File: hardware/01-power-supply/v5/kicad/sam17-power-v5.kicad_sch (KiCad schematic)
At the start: 208 parts, among them J1 Bornera 2P 5.0 mm, J10 PinHeader 1x04, J2 Molex KK-254 4P, J3 Bornera 4P 5.08 mm, J5 Faston 6.3x0.8 PCB, J6 Molex KK-254 2P, J7 Molex KK-254 4P, J8 PinHeader 1x04, J9 Molex KK-254 2P, Q2 CSD18534Q5A, Q3 MMBT3906, Q4 MMBT3906, Q5 MMBT3906, Q6 MMBT3906, SW1 Pulsador 6x6, U1 LT1963AEQ, U10 ADS1115IDGS, U11 TMP1075DGK, U12 INA226, U13 INA226, U14 INA226, U15 LM74502DDFR, U16 TPS26631PWPR, U17 MSP430FR2111IPW16, U18 TPS70933DBVR, U19 TPS26631PWPR, U2 LT3015EQ, U20 LM393B, U21 TL431BI, U22 TL431BI, U23 TL431BI, U24 TL431BI, U25 TL431BI, U4 LT3045EDD, U5 LT3045EDD, U6 LT3094EDD, U7 LT3094EDD, U8 INA226, U9 ISO1541

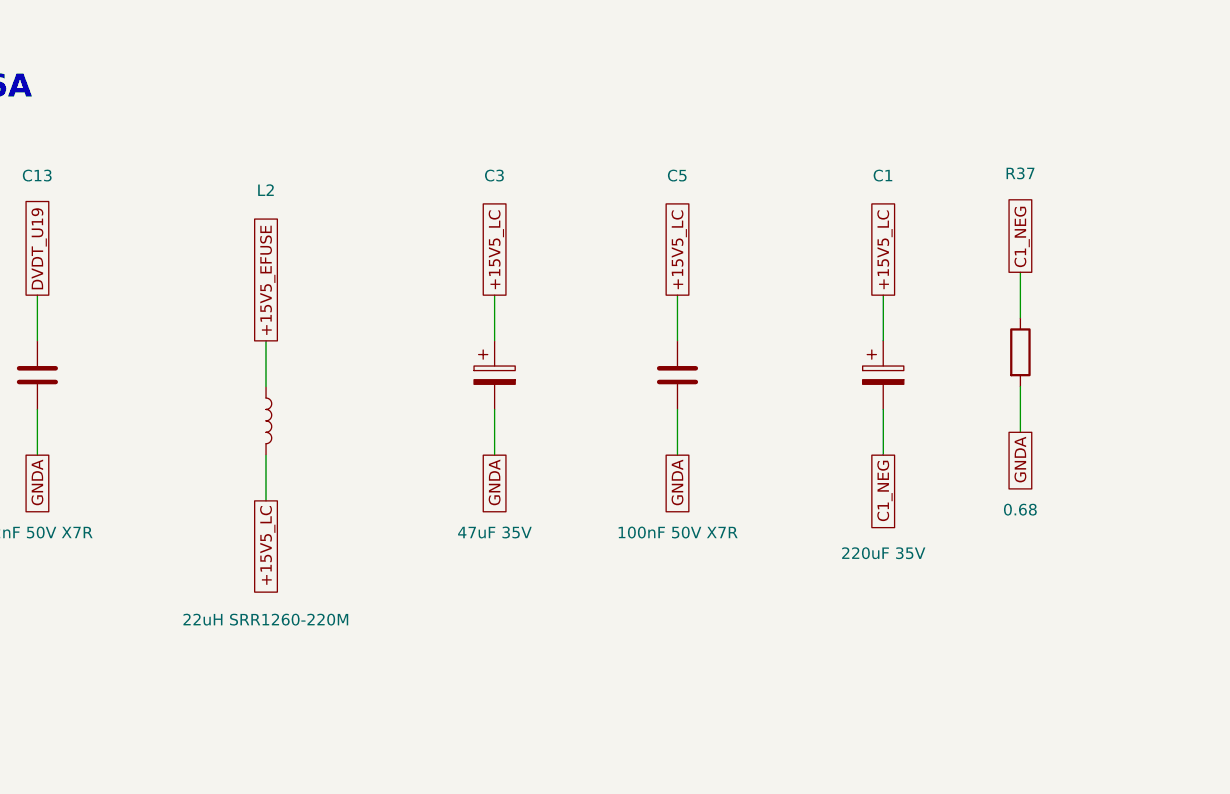
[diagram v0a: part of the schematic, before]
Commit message: hardware: fuente v5, placa y fabricacion con L2 en SRP1265A-220M
Placa colocada y ruteada de nuevo: Freerouting en 3 rondas y el rescate
cierra las 7 conexiones que deja abiertas. L2 sigue en (97, 48); su
cuerpo pasa de 12,5 a 13,5 mm en x.

build_pcb.py: Freerouting salio de U4.9 por su cuenta y puso la via a
mitad de la salida fija de OUTS_POS, con 0,8 mm de punta colgando.
limpiar_colgantes() ya no deja asi una pista fija: la recorta hasta el
ultimo contacto de su red (_recortar), y lo de antes no cambia.

- 1510 pistas y 284 vias (263 de 0,6/0,3 mm y 21 de 0,8/0,4 mm).
- Bajo el cuerpo de L2 pasan ahora +15V5_FILT en F.Cu, entre sus pads, y
  SCL_A/SDA_A en In2, debajo del plano de In1.
- DRC (kicad-cli 10.0.3, todas las severidades, zonas rellenas y paridad
  con el esquematico): 0 infracciones, 0 sin conectar, 0 de paridad.
- Ocho referencias van solo en F.Fab: entran R43, R70, R71 y FB1, y R40
  y R67 vuelven a la serigrafia.

Esquematico, netlist, fab/ y pcb/ regenerados.
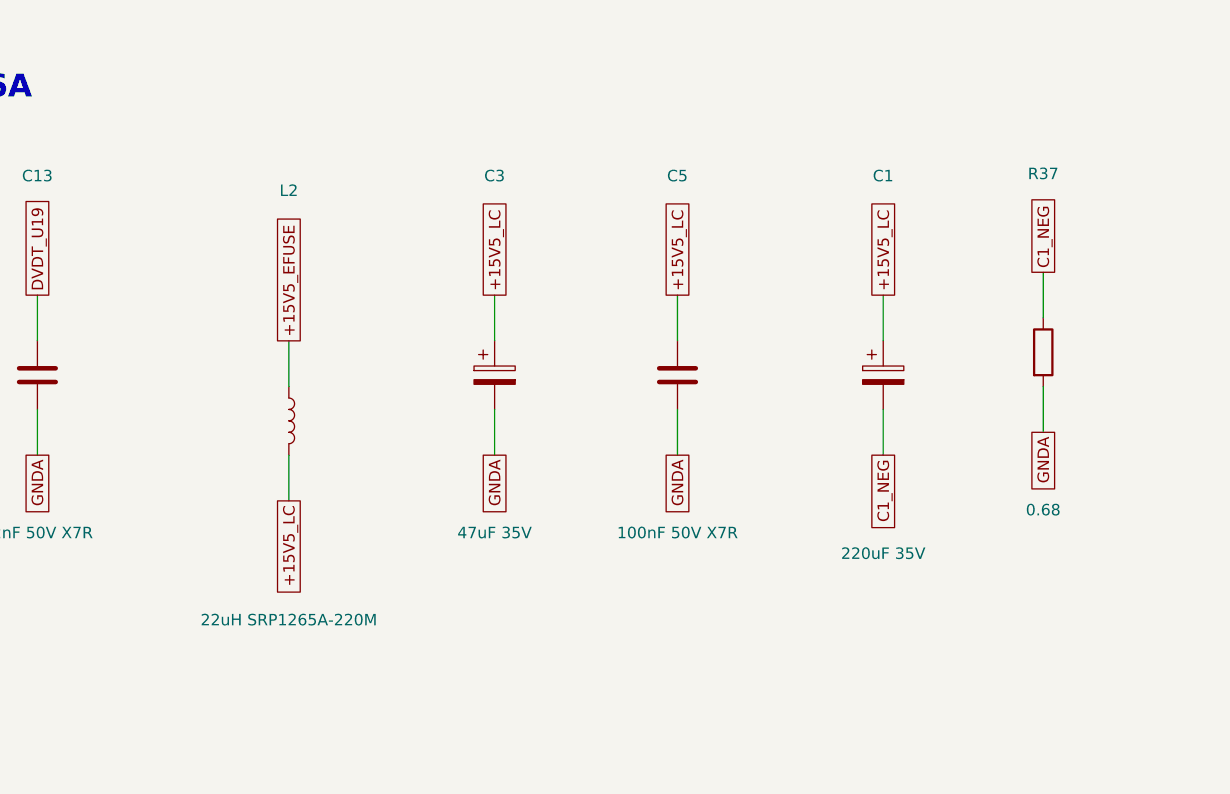
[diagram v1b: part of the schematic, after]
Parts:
- L2: value 22uH SRR1260-220M -> 22uH SRP1265A-220M; footprint Inductor_SMD:L_Bourns_SRR1260 -> sam17:L_Bourns_SRP1265A; LCSC C3224283 -> C2041465; MPN SRR1260-220M -> SRP1265A-220M
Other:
- moved on the sheet: L2, R37
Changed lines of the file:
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@@
 	(wire
 		(pts
-			(xy 241.3 422.91) (xy 241.3 417.83)
+			(xy 243.84 422.91) (xy 243.84 417.83)
 		)
 		(stroke
@@
 	(wire
 		(pts
-			(xy 241.3 430.53) (xy 241.3 435.61)
+			(xy 243.84 430.53) (xy 243.84 435.61)
 		)
 		(stroke
@@
 	(wire
 		(pts
-			(xy 325.12 415.29) (xy 325.12 410.21)
+			(xy 327.66 415.29) (xy 327.66 410.21)
 		)
 		(stroke
@@
 	(wire
 		(pts
-			(xy 325.12 422.91) (xy 325.12 427.99)
+			(xy 327.66 422.91) (xy 327.66 427.99)
 		)
 		(stroke
@@
 	(global_label "+15V5_EFUSE"
 		(shape passive)
-		(at 241.3 417.83 90)
+		(at 243.84 417.83 90)
 		(effects
 			(font
@@
 	(global_label "+15V5_LC"
 		(shape passive)
-		(at 241.3 435.61 270)
+		(at 243.84 435.61 270)
 		(effects
 			(font
@@
 	(global_label "C1_NEG"
 		(shape passive)
-		(at 325.12 410.21 90)
+		(at 327.66 410.21 90)
 		(effects
 			(font
@@
 	(global_label "GNDA"
 		(shape passive)
-		(at 325.12 427.99 270)
+		(at 327.66 427.99 270)
 		(effects
 			(font
@@
 	(symbol
 		(lib_id "Device:L")
-		(at 241.3 426.72 0)
+		(at 243.84 426.72 0)
 		(unit 1)
 		(exclude_from_sim no)
@@
 		(dnp no)
 		(property "Reference" "L2"
-			(at 241.3 401.14 0)
+			(at 243.84 401.14 0)
 			(show_name no)
 			(do_not_autoplace no)
@@
 			)
 		)
-		(property "Value" "22uH SRR1260-220M"
-			(at 241.3 448.85 0)
+		(property "Value" "22uH SRP1265A-220M"
+			(at 243.84 448.85 0)
 			(show_name no)
 			(do_not_autoplace no)
@@
 			)
 		)
-		(property "Footprint" "Inductor_SMD:L_Bourns_SRR1260"
-			(at 241.3 426.72 0)
+		(property "Footprint" "sam17:L_Bourns_SRP1265A"
+			(at 243.84 426.72 0)
 			(hide yes)
 			(show_name no)
@@
 		)
 		(property "Datasheet" ""
-			(at 241.3 426.72 0)
+			(at 243.84 426.72 0)
 			(hide yes)
 			(show_name no)
@@
 		)
 		(property "Description" ""
-			(at 241.3 426.72 0)
+			(at 243.84 426.72 0)
 			(hide yes)
 			(show_name no)
@@
 			)
 		)
-		(property "LCSC" "C3224283"
-			(at 241.3 426.72 0)
+		(property "LCSC" "C2041465"
+			(at 243.84 426.72 0)
 			(hide yes)
 			(show_name no)
@@
 			)
 		)
-		(property "MPN" "SRR1260-220M"
-			(at 241.3 426.72 0)
+		(property "MPN" "SRP1265A-220M"
+			(at 243.84 426.72 0)
 			(hide yes)
 			(show_name no)
@@
 	(symbol
 		(lib_id "Device:R")
-		(at 325.12 419.1 0)
+		(at 327.66 419.1 0)
 		(unit 1)
 		(exclude_from_sim no)
@@
 		(dnp no)
 		(property "Reference" "R37"
-			(at 325.12 399.27 0)
+			(at 327.66 399.27 0)
 			(show_name no)
 			(do_not_autoplace no)
@@
 		)
 		(property "Value" "0.68"
-			(at 325.12 436.63 0)
+			(at 327.66 436.63 0)
 			(show_name no)
 			(do_not_autoplace no)
@@
 		)
 		(property "Footprint" "Resistor_SMD:R_1206_3216Metric"
-			(at 325.12 419.1 0)
+			(at 327.66 419.1 0)
 			(hide yes)
 			(show_name no)
@@
 		)
 		(property "Datasheet" ""
-			(at 325.12 419.1 0)
+			(at 327.66 419.1 0)
 			(hide yes)
 			(show_name no)
@@
 		)
 		(property "Description" ""
-			(at 325.12 419.1 0)
+			(at 327.66 419.1 0)
 			(hide yes)
 			(show_name no)
@@
 		)
 		(property "LCSC" "C19108"
-			(at 325.12 419.1 0)
+			(at 327.66 419.1 0)
 			(hide yes)
 			(show_name no)
@@
 		)
 		(property "MPN" "1206W4F680LT5E"
-			(at 325.12 419.1 0)
+			(at 327.66 419.1 0)
 			(hide yes)
 			(show_name no)

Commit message: fix(fuente-v5): PS3 a THN 20-2411WI aislado, con C39 y +5V_AUX tras F4
El K7805T de PS3 era un buck no aislado: con la entrada puenteada a la
salida, +5V_AUX pasaba de los 6,0 V de los INA226 y del ISO1541. En el
THN 20-2411WI la entrada y la salida solo se tocan por la barrera de
1600 VDC, el camino que la propuesta de piezas (sec. 9.1) deja fuera del
contrato de fallo simple.

- C39, 1000 uF / 16 V (Lelon VZH102M1CTR-1010, C249844): con el THN a su
  limite la subida del riel baja a 0,0095 V/us y el pico queda en 5,88 V.
- +5V_AUX cuelga de +5V_FUSED_RACK: si F4 abre tras el disparo, se apaga
  en vez de quedarse con el OVP del THN (hasta 8,20 V).
- R49 = 12,7 kohm: SCR3 dispara entre 5,53 y 5,86 V.
- check_absmax.py: fuga_ps3() con su guarda y sus canarios, y la fila de
  +5V_AUX en absmax.csv. check_netlist.py fija la toma de R20 tras F4.
- Placa reruteada: PS3 en la columna de convertidores, PS2 abajo, NT1
  entre PS5 y PS3, GNDA por la derecha de PS3 y C39. DRC 0, 0 sin conectar.
- Presupuestos: derating del 2411WI, 83 % al 20 % de carga (el cajon pasa
  a 65,31 W), medidas.csv.
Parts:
- removed C15: 10uF 50V X7R, Capacitor_SMD:C_1210_3225Metric, symbol Device:C
- added C39: 1000uF 16V, Capacitor_SMD:CP_Elec_10x10, symbol Device:C_Polarized
- PS3: value K7805T-1000R3 -> THN 20-2411WI; footprint sam17:Converter_DCDC_Mornsun_K78_T-1000R3_SMD -> Converter_DCDC:Converter_DCDC_TRACO_THL30-xxxxWI_THT; symbol sam17:Mornsun_K78xxT-1000R3 -> sam17:TRACO_THN_Single; MPN K7805T-1000R3 -> THN 20-2411WI
- R49: value 13.3k 0.1% -> 12.7k 0.1%; LCSC C865182 -> C50670219; MPN RT0805BRD0713K3L -> TC0525B1272T5G
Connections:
- net +24V_SW: no longer PS3.2 (+Vin)
- net +5V_FUSED_RACK: now also R20.1, U12.10 (Vin+)
- net +5V_RAW_RACK: now also PS3.3 (+Vout), C39.1; no longer PS3.4 (+Vout), PS3.5 (+Vout), R20.1, U12.10 (Vin+)
- net GND24: now also PS3.2 (-Vin); no longer C16.2, PS3.3 (GND), PS3.7 (GND)
- net GNDA: now also C16.2, PS3.5 (-Vout), C39.2
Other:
- note added: "BLOQUE DCDC: Convertidores: THN 30 (+-12 rack), URB (+5 digital M1), 3 x THN 20 (+5 rack, +-15.5)"
- note removed: "BLOQUE DCDC: Convertidores: THN 30 (+-12 rack), URB (+5 digital M1), K78 (+5 rack), 2 x THN 20 (+-15.5)"
- moved on the sheet: C16, C2, C22, C24, C25, C26, C28, C35, C37, C4, C6, D10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

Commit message: feat(fuente-v5): placa y ficheros de fabricacion con Q7 en el retorno
Regenerados con build_schematic.py, build_pcb.py y build_fab.py: DRC con
todas las severidades y paridad con el esquematico en 0 infracciones, 0 sin
conectar y 0 diferencias de paridad; 1464 pistas y 294 vias (271 de 0,6 mm y
23 de 0,8 mm).

- Q7 sobre J1.2 (rot 270, drenador abajo) y D1 a su lado; la isla
  RET24_RAW (J1.2, D1.2 y el drenador de Q7) es cobre fijo de >= 2,4 mm que
  los vertidos de GND24 rodean sin tocar, y las tres fuentes de Q7 van
  juntas a GND24 por cobre de 1,8 mm. R85 y D20 quedan junto a D1.
- L3 en la huella de la SRP1265A (13,5 x 12,5 mm).
- fab/: gerbers, taladros y posiciones; el BOM y el CPL de JLC pierden D10 y
  D12 (sin montar) y ganan Q7, D20 y R85. Nueve referencias solo en F.Fab.
- sam17-power-v5.net, .kicad_sch, esquemas y vistas de la placa.
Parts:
- added D20: BZT52C15, Diode_SMD:D_SOD-123, symbol Device:D_Zener
- added Q7: CSD18534Q5A, Package_TO_SOT_SMD:TDSON-8-1, symbol Transistor_FET:CSD18534Q5A
- added R85: 10k, Resistor_SMD:R_0805_2012Metric, symbol Device:R
- C10: value 100nF 50V X7R -> 100nF 100V X7R; LCSC C49678 -> C106243; MPN CC0805KRX7R9BB104 -> CC0805KKX7R0BB104
- D1: value SMBJ26CA -> SMBJ33CA; LCSC C83332 -> C83325; MPN SMBJ26CA -> SMBJ33CA
- L3: value 22uH SRR1260-220M -> 22uH SRP1265A-220M; footprint Inductor_SMD:L_Bourns_SRR1260 -> sam17:L_Bourns_SRP1265A; LCSC C3224283 -> C2041465; MPN SRR1260-220M -> SRP1265A-220M
- R32, R33: value 45.3k -> 45.3k 0.1%; LCSC C17701 -> C866072; MPN 0805W8F4532T5E -> RT0805BRE0745K3L
- R64: value 1k -> 1.2k; LCSC C17513 -> C17379; MPN 0805W8F1001T5E -> 0805W8F1201T5E
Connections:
- net +24V_RAW: now also R85.1
- net GND24: now also D20.2 (A), Q7.1 (S), Q7.2 (S), Q7.3 (S); no longer D1.2 (A2), J1.2 (Pin_2)
- new net G_Q7: D20.1 (K), Q7.4 (G), R85.2
- new net RET24_RAW: D1.2 (A2), J1.2 (Pin_2), Q7.5 (D)
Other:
- note added: "BLOQUE M5: Entrada 24 V, polaridad (LM74502 + 2 x CSD18534Q5A, +24 V y retorno), eFuse U16 y supervisor M5"
- note removed: "BLOQUE M5: Entrada 24 V, polaridad (LM74502 + CSD18534Q5A), eFuse U16 y supervisor M5"
- moved on the sheet: C10, C11, C12, C23, C6, C7, C8, C9, D11, D18, D2, J10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

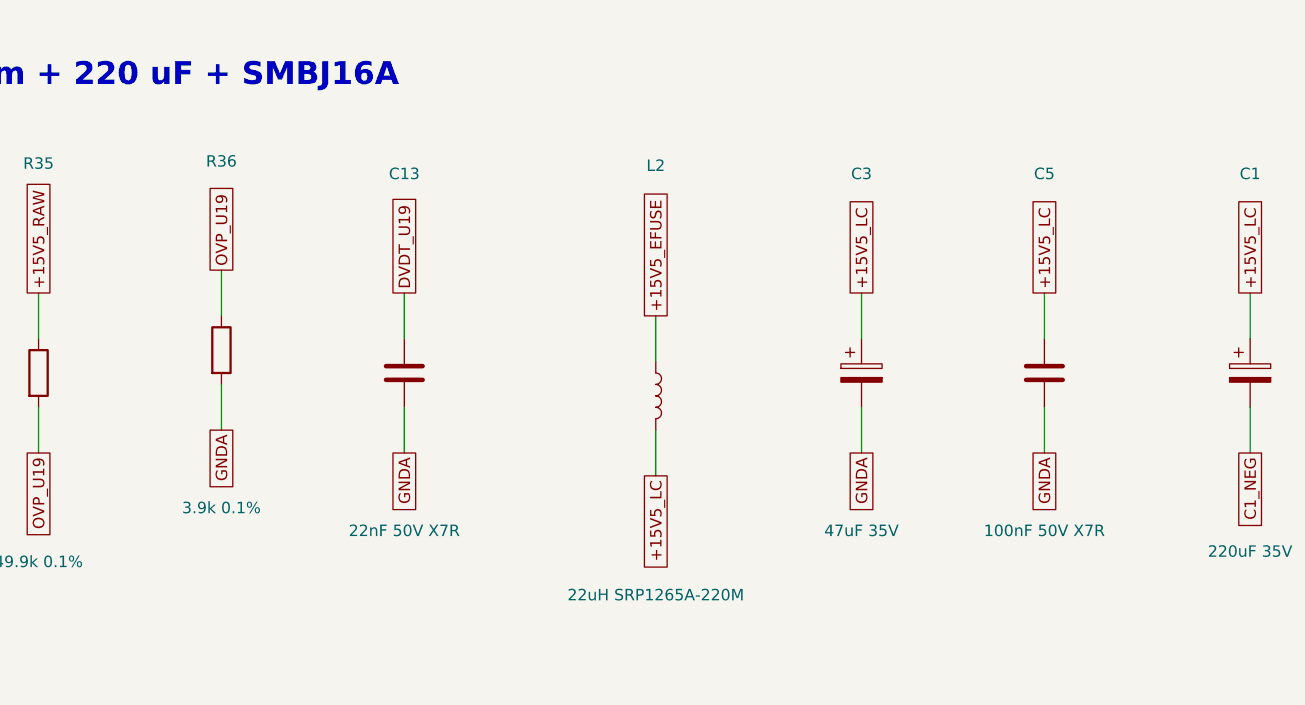
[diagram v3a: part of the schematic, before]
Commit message: fuente-v5: R36 a 3,74 kohm, el OVP de U19 deja sitio al sobreimpulso del THN
R36 pasa de 3,9 kohm a 3,74 kohm 0,1 % (Yageo RT0805BRD073K74L, C865467,
misma serie y huella). El OVP de U19 sube de 16,55 a 17,21 V nominal, con
banda de 16,83 a 17,59 V: el margen sobre el THN sano pasa de 0,18 a 0,82 V
en la envolvente de margen_budget.py, y el sobreimpulso tipico al soltar
carga (~0,19 V) cabe.

Con el borde alto por encima del pico de #334 (17,40 V), lo peor que ve U1
es un THN atascado justo debajo del OVP. check_absmax.py toma el mayor de
los dos en absmax.csv, en la guarda de D10 y en su canario; D10 sigue sin
conducir (17,59 V contra V_BR 17,8 V).

La spec v5 y la propuesta de piezas llevan la banda nueva y las cifras del
disparo rapido (3,32 A, 7,5 us). Placa regenerada con --desde-ruteo: mismo
ruteo, DRC en 0.
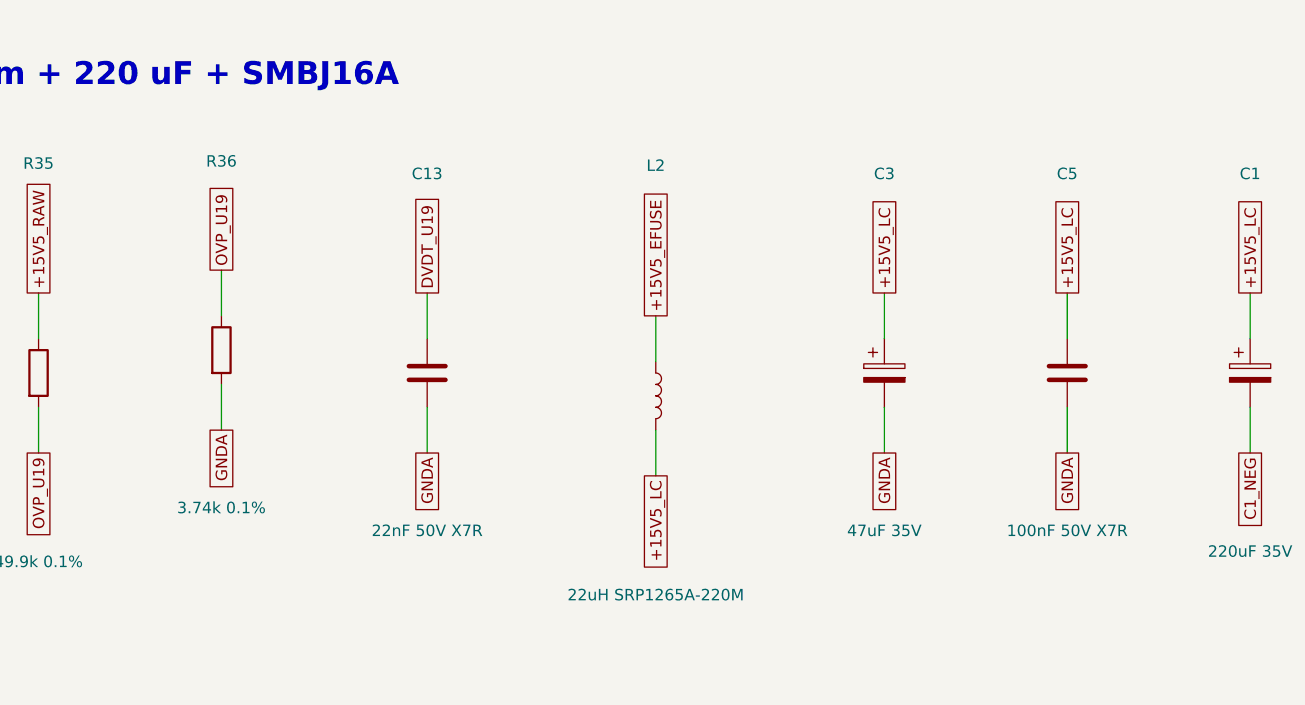
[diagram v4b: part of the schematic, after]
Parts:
- R36: value 3.9k 0.1% -> 3.74k 0.1%; LCSC C865471 -> C865467; MPN RT0805BRD073K9L -> RT0805BRD073K74L
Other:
- moved on the sheet: C13, C3, C5
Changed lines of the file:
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@@
 	(wire
 		(pts
-			(xy 215.9 417.83) (xy 215.9 412.75)
+			(xy 218.44 417.83) (xy 218.44 412.75)
 		)
 		(stroke
@@
 	(wire
 		(pts
-			(xy 215.9 425.45) (xy 215.9 430.53)
+			(xy 218.44 425.45) (xy 218.44 430.53)
 		)
 		(stroke
@@
 	(wire
 		(pts
-			(xy 266.7 417.83) (xy 266.7 412.75)
+			(xy 269.24 417.83) (xy 269.24 412.75)
 		)
 		(stroke
@@
 	(wire
 		(pts
-			(xy 266.7 425.45) (xy 266.7 430.53)
+			(xy 269.24 425.45) (xy 269.24 430.53)
 		)
 		(stroke
@@
 	(wire
 		(pts
-			(xy 287.02 417.83) (xy 287.02 412.75)
+			(xy 289.56 417.83) (xy 289.56 412.75)
 		)
 		(stroke
@@
 	(wire
 		(pts
-			(xy 287.02 425.45) (xy 287.02 430.53)
+			(xy 289.56 425.45) (xy 289.56 430.53)
 		)
 		(stroke
@@
 	(global_label "DVDT_U19"
 		(shape passive)
-		(at 215.9 412.75 90)
+		(at 218.44 412.75 90)
 		(effects
 			(font
@@
 	(global_label "GNDA"
 		(shape passive)
-		(at 215.9 430.53 270)
+		(at 218.44 430.53 270)
 		(effects
 			(font
@@
 	(global_label "+15V5_LC"
 		(shape passive)
-		(at 266.7 412.75 90)
+		(at 269.24 412.75 90)
 		(effects
 			(font
@@
 	(global_label "GNDA"
 		(shape passive)
-		(at 266.7 430.53 270)
+		(at 269.24 430.53 270)
 		(effects
 			(font
@@
 	(global_label "+15V5_LC"
 		(shape passive)
-		(at 287.02 412.75 90)
+		(at 289.56 412.75 90)
 		(effects
 			(font
@@
 	(global_label "GNDA"
 		(shape passive)
-		(at 287.02 430.53 270)
+		(at 289.56 430.53 270)
 		(effects
 			(font
@@
 			)
 		)
-		(property "Value" "3.9k 0.1%"
+		(property "Value" "3.74k 0.1%"
 			(at 195.58 436.63 0)
 			(show_name no)
@@
 			)
 		)
-		(property "LCSC" "C865471"
+		(property "LCSC" "C865467"
 			(at 195.58 419.1 0)
 			(hide yes)
@@
 			)
 		)
-		(property "MPN" "RT0805BRD073K9L"
+		(property "MPN" "RT0805BRD073K74L"
 			(at 195.58 419.1 0)
 			(hide yes)
@@
 	(symbol
 		(lib_id "Device:C")
-		(at 215.9 421.64 0)
+		(at 218.44 421.64 0)
 		(unit 1)
 		(exclude_from_sim no)
@@
 		(dnp no)
 		(property "Reference" "C13"
-			(at 215.9 399.51 0)
+			(at 218.44 399.51 0)
 			(show_name no)
 			(do_not_autoplace no)
@@
 		)
 		(property "Value" "22nF 50V X7R"
-			(at 215.9 439.17 0)
+			(at 218.44 439.17 0)
 			(show_name no)
 			(do_not_autoplace no)
@@
 		)
 		(property "Footprint" "Capacitor_SMD:C_0805_2012Metric"
-			(at 215.9 421.64 0)
+			(at 218.44 421.64 0)
 			(hide yes)
 			(show_name no)
@@
 		)
 		(property "Datasheet" ""
-			(at 215.9 421.64 0)
+			(at 218.44 421.64 0)
 			(hide yes)
 			(show_name no)
@@
 		)
 		(property "Description" ""
-			(at 215.9 421.64 0)
+			(at 218.44 421.64 0)
 			(hide yes)
 			(show_name no)
@@
 		)
 		(property "LCSC" "C1729"
-			(at 215.9 421.64 0)
+			(at 218.44 421.64 0)
 			(hide yes)
 			(show_name no)
@@
 		)
 		(property "MPN" "CL21B223KBANNNC"
-			(at 215.9 421.64 0)
+			(at 218.44 421.64 0)
 			(hide yes)
 			(show_name no)
@@
 	(symbol
 		(lib_id "Device:C_Polarized")
-		(at 266.7 421.64 0)
+		(at 269.24 421.64 0)
 		(unit 1)
 		(exclude_from_sim no)
@@
 		(dnp no)
 		(property "Reference" "C3"
-			(at 266.7 399.51 0)
+			(at 269.24 399.51 0)
 			(show_name no)
 			(do_not_autoplace no)
@@
 		)
 		(property "Value" "47uF 35V"
-			(at 266.7 439.17 0)
+			(at 269.24 439.17 0)
 			(show_name no)
 			(do_not_autoplace no)
@@
 		)
 		(property "Footprint" "Capacitor_SMD:CP_Elec_6.3x7.7"
-			(at 266.7 421.64 0)
+			(at 269.24 421.64 0)
 			(hide yes)
 			(show_name no)
@@
 		)
 		(property "Datasheet" ""
-			(at 266.7 421.64 0)
+			(at 269.24 421.64 0)
 			(hide yes)
 			(show_name no)
@@
 		)
 		(property "Description" ""
-			(at 266.7 421.64 0)
+			(at 269.24 421.64 0)
 			(hide yes)
 			(show_name no)
@@
 		)
 		(property "LCSC" "C249923"
-			(at 266.7 421.64 0)
+			(at 269.24 421.64 0)
 			(hide yes)
 			(show_name no)
@@
 		)
 		(property "MPN" "VZH470M1VTR-0607"
-			(at 266.7 421.64 0)
+			(at 269.24 421.64 0)
 			(hide yes)
 			(show_name no)
@@
 	(symbol
 		(lib_id "Device:C")
-		(at 287.02 421.64 0)
+		(at 289.56 421.64 0)
 		(unit 1)
 		(exclude_from_sim no)
@@
 		(dnp no)
 		(property "Reference" "C5"
-			(at 287.02 399.51 0)
+			(at 289.56 399.51 0)
 			(show_name no)
 			(do_not_autoplace no)
@@
 		)
 		(property "Value" "100nF 50V X7R"
-			(at 287.02 439.17 0)
+			(at 289.56 439.17 0)
 			(show_name no)
 			(do_not_autoplace no)
@@
 		)
 		(property "Footprint" "Capacitor_SMD:C_0805_2012Metric"
-			(at 287.02 421.64 0)
+			(at 289.56 421.64 0)
 			(hide yes)
 			(show_name no)
@@
 		)
 		(property "Datasheet" ""
-			(at 287.02 421.64 0)
+			(at 289.56 421.64 0)
 			(hide yes)
 			(show_name no)
@@
 		)
 		(property "Description" ""
-			(at 287.02 421.64 0)
+			(at 289.56 421.64 0)
 			(hide yes)
 			(show_name no)
@@
 		)
 		(property "LCSC" "C49678"
-			(at 287.02 421.64 0)
+			(at 289.56 421.64 0)
 			(hide yes)
 			(show_name no)
@@
 		)
 		(property "MPN" "CC0805KRX7R9BB104"
-			(at 287.02 421.64 0)
+			(at 289.56 421.64 0)
 			(hide yes)
 			(show_name no)
